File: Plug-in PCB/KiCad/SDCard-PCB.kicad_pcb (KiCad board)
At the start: 4 copper layers, 37.5 x 40 mm, 76 parts, among them J1 Conn_01x01, J10 Conn_01x01, J11 Conn_01x01, J12 Conn_01x01, J13 Conn_01x01, J14 Conn_01x01, J15 Conn_01x08, J16 Conn_01x01, J17 Conn_01x01, J18 Conn_01x01, J19 Conn_01x01, J2 Conn_01x01, J3 Conn_01x01, J4 Conn_01x01, J5 Conn_01x01, J6 Conn_01x01, J7 Conn_01x01, J8 Conn_Coaxial, J9 Conn_01x05, U1 DS90UB933-Q1, U2 TLV7103318DSER, U4 ATSAME70N21A-CN, Y1 ABM8G-12.000MHZ-4Y-T3

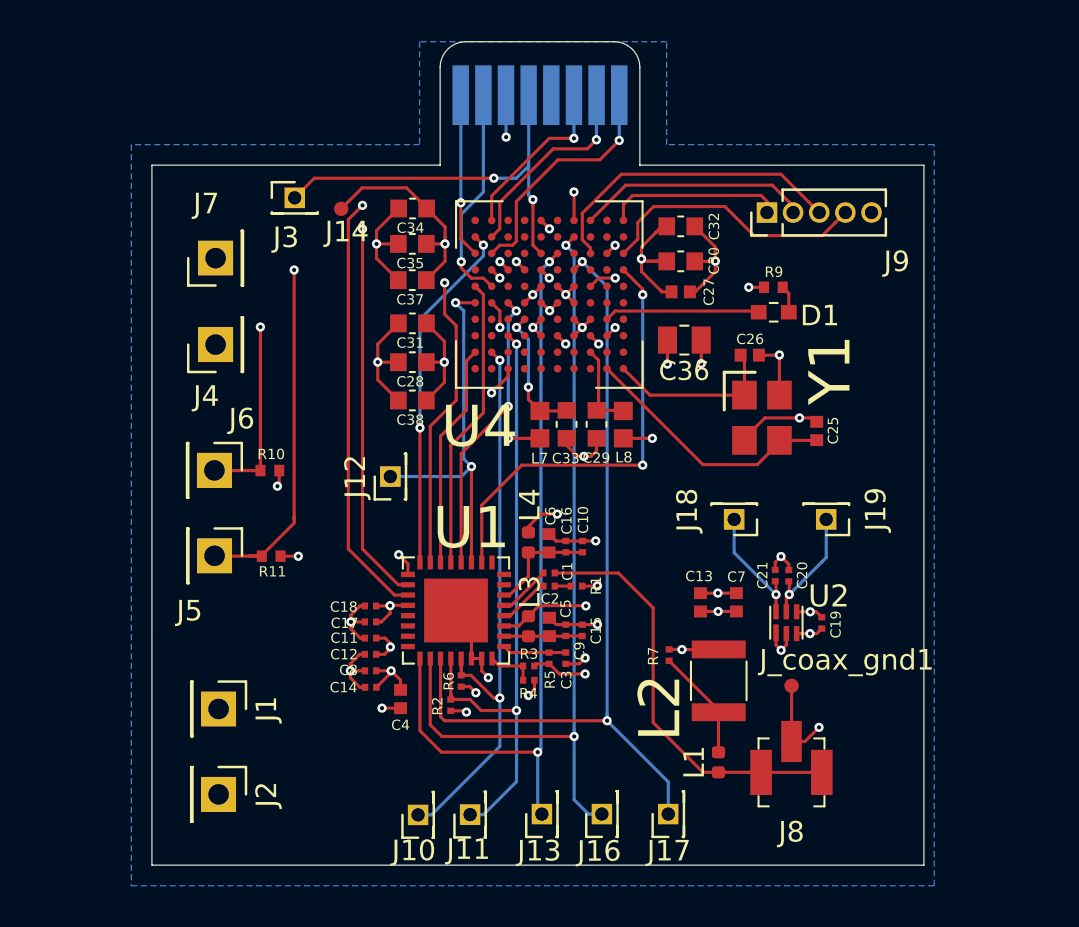
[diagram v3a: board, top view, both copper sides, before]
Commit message: Change MCU and Serializer Power to 3.3V
1. MCU VDDIO, SWD, VDDIN, VDDUTMII powered at 3.3V

2. Serializer VDDIO, PDB powered at 3.3V

3. Layout changed (Pins enlarged, Coax_Gnd added, Coax connector moved closer to seralizer)
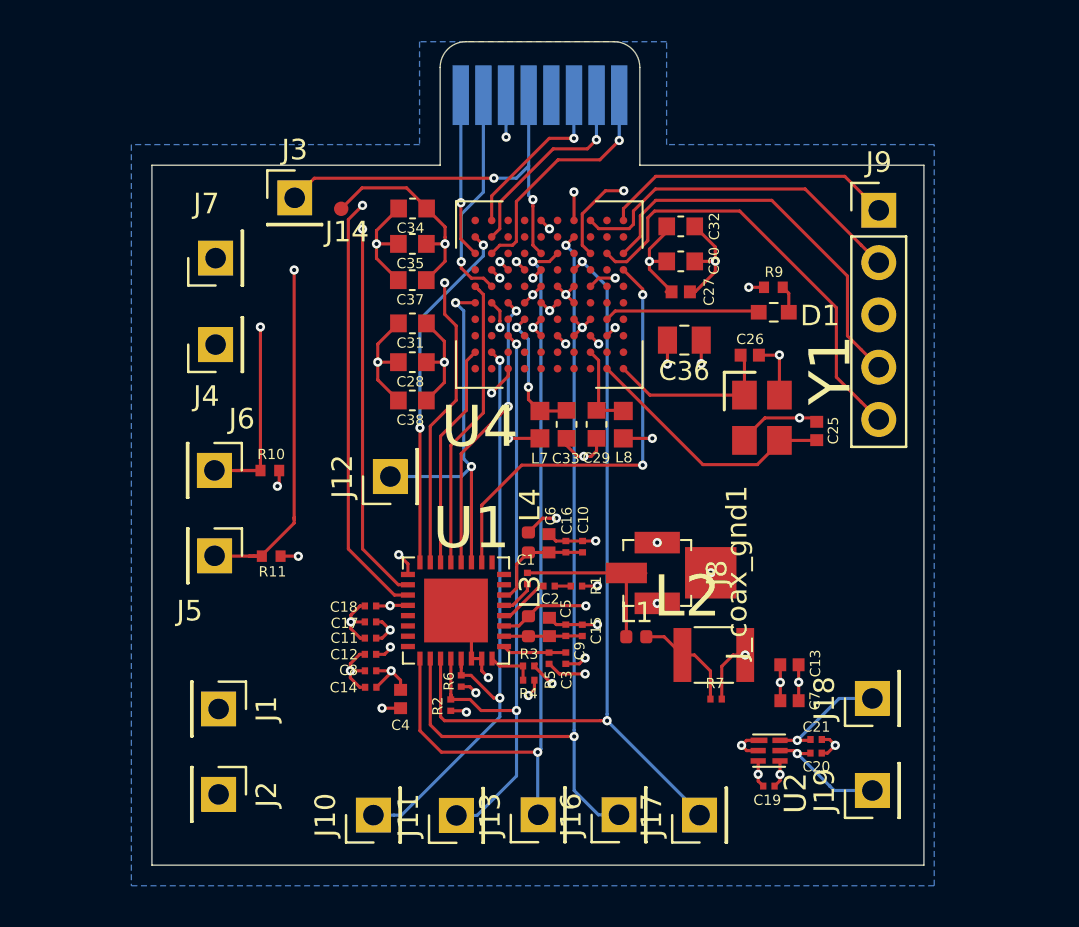
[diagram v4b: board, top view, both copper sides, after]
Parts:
- J10, J11, J12, J13, J16, J17, J18, J19, J3: footprint Connector_PinHeader_1.27mm:PinHeader_1x01_P1.27mm_Vertical -> Connector_PinHeader_2.54mm:PinHeader_1x01_P2.54mm_Vertical
- J9: footprint Connector_PinHeader_1.27mm:PinHeader_1x05_P1.27mm_Vertical -> Connector_PinHeader_2.54mm:PinHeader_1x05_P2.54mm_Vertical
- J_coax_gnd1: footprint .Connector:Conn_1x1_700_Circular_Pad -> .Connector:Conn_1x1_1mmx1mm_Pad
- moved J19 13.4 mm to (135.0, 83.4), turned to 90 degrees
- moved J8 11.7 mm to (124.7, 72.8), turned to 270 degrees
- moved J18 11.0 mm to (135.0, 78.9), turned to 90 degrees
- moved C20 8.72 mm to (132.3, 81.6), turned to 0 degrees
- moved C19 8.33 mm to (130.0, 83.2), turned to 0 degrees
- moved C21 8.21 mm to (132.3, 80.9), turned to 0 degrees
- moved L1 7.29 mm to (123.5, 75.9), turned to 0 degrees
- moved J_coax_gnd1 6.75 mm to (127.1, 72.8), turned to 90 degrees
- moved U2 6.27 mm to (130.0, 81.4), turned to 270 degrees
- moved C7 5.43 mm to (131.0, 79.0), turned to 0 degrees
- moved J9 5.43 mm to (135.3, 55.2), turned to 0 degrees
- moved C13 5.28 mm to (131.0, 77.3), turned to 0 degrees
- moved R7 3.13 mm to (127.4, 78.9), turned to 180 degrees
- moved J10 2.17 mm to (110.8, 84.6)
- moved J17 1.52 mm to (126.6, 84.6)
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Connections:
- C11 pad 1: +1V8 -> +3V3
- C17 pad 1: +1V8 -> +3V3
- C27 pad 1: +1V8 -> +3V3
- C28 pad 1: +1V8 -> +3V3
- C30 pad 1: +1V8 -> +3V3
- C31 pad 1: +1V8 -> +3V3
- C32 pad 1: +1V8 -> +3V3
- C38 pad 1: +1V8 -> +3V3
- J4 pad 1: +1V8 -> +3V3
- J8 pad 1: /Serializer/DOUT_P -> Earth
- J8 pad 2: Earth -> /Serializer/DOUT_P
- R10 pad 1: +1V8 -> +3V3
- R11 pad 1: +1V8 -> +3V3
- R5 pad 1: +1V8 -> +3V3
- U1 pad 25: +1V8 -> +3V3
- U4 pad C2: +1V8 -> +3V3
- U4 pad C5: +1V8 -> +3V3
- U4 pad E5: +1V8 -> +3V3
- U4 pad E6: +1V8 -> +3V3
- U4 pad F3: +1V8 -> +3V3
- U4 pad G7: +1V8 -> +3V3
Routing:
- net +1V8: track 42.7 -> 18.8 mm, vias 17 -> 7
- net +3V3: track 7.61 -> 28.7 mm, vias 3 -> 15
- net /Serializer/DOUT_P: track 20.3 -> 7.92 mm
- net /OnBoardMCU/test5: track 13.7 -> 21.2 mm, vias 1 -> 0
- net /OnBoardMCU/test4: track 13.2 -> 19.1 mm
- net /OnBoardMCU/test1: track 8.58 -> 14.3 mm
- net /OnBoardMCU/test2: track 11.3 -> 16.8 mm
- net Earth: track 64.0 -> 59.7 mm, vias 26 -> 28
- net /OnBoardMCU/test3: track 15.2 -> 19.4 mm, vias 0 -> 1
- net /OnBoardMCU/SDA: track 28.2 -> 29.6 mm
- net /OnBoardMCU/LINE_VALID: track 37.4 -> 38.4 mm
- net Net-(C1-Pad2): track 2.57 -> 1.74 mm
- net /OnBoardMCU/PXL_CLK: track 40.1 -> 40.8 mm
- net /OnBoardMCU/FRAME_VALID: track 39.7 -> 40.3 mm
- net /OnBoardMCU/SCL: track 30.3 -> 30.8 mm
- added copper zone on In2.Cu, net +1V8
- added copper zone on B.Cu, net +3V3
- removed copper zone on B.Cu, net +1V8
- removed copper zone on In2.Cu, net +3V3
